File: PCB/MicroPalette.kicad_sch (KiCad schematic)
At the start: 5 parts, among them J1 Conn_01x07_Pin, J2 Conn_01x04_Pin, U1 XIAO-RP2040-DIP

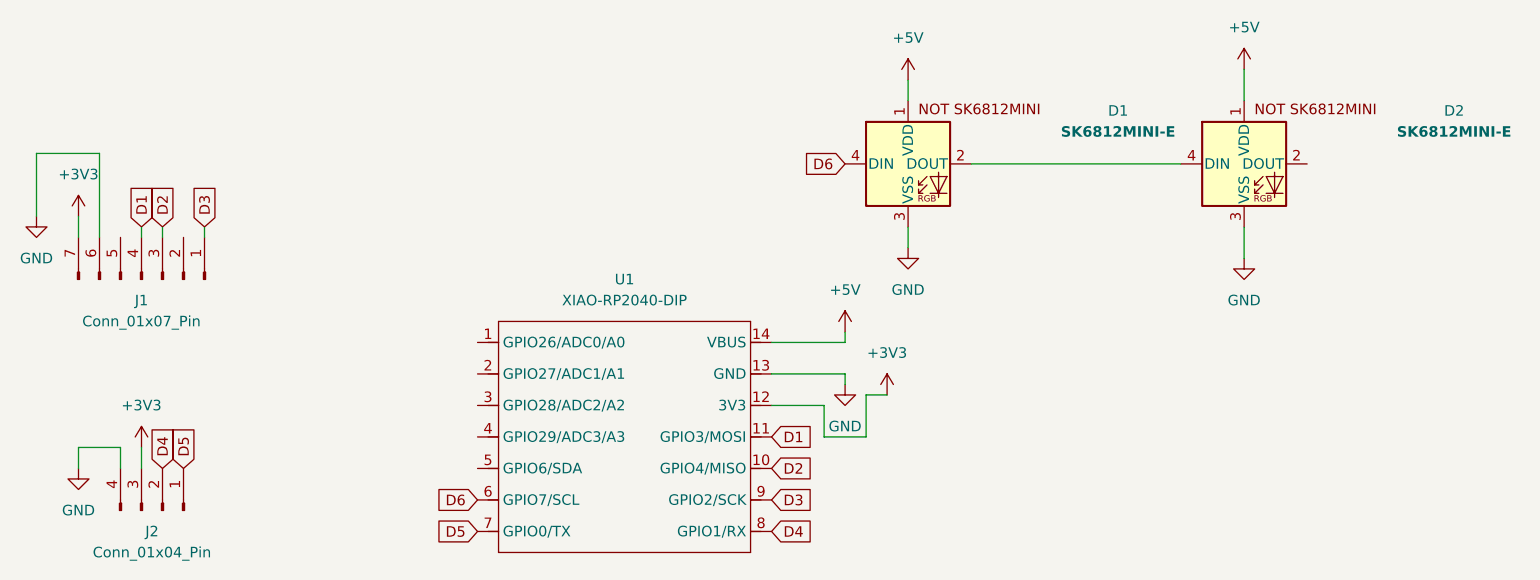
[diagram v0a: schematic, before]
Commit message: Add files via upload
fixed pcb, sda/scl was wrong in the previous version
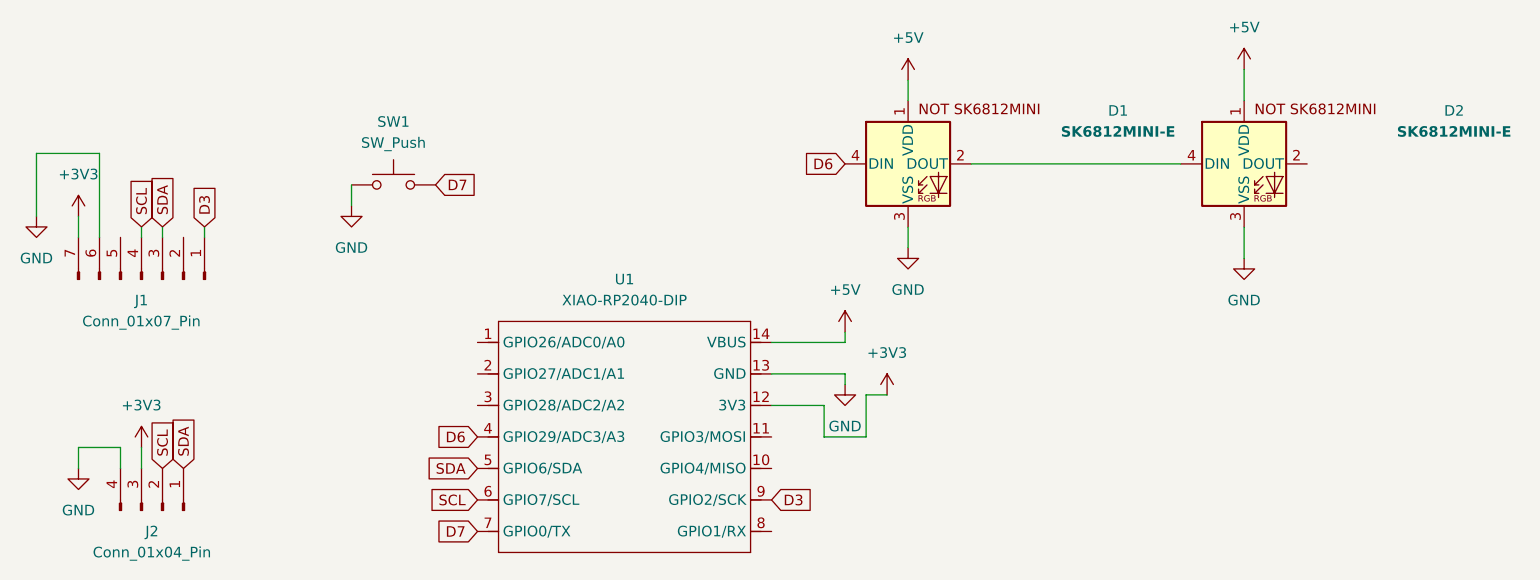
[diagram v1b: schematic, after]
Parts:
- added SW1: SW_Push, Button_Switch_Keyboard:SW_Cherry_MX_1.00u_PCB, symbol Switch:SW_Push
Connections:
- net D6: now also U1.4 (GPIO29/ADC3/A3); no longer U1.6 (GPIO7/SCL)
- net GND: now also SW1.1
- net SDA: now reaches U1.5 (GPIO6/SDA)
- net SDA: now also J1.3 (Pin_3), J2.1 (Pin_1)
- net D1: no longer names the net of U1.11 (GPIO3/MOSI)
- net D1: no longer J1.4 (Pin_4)
- net D2: no longer names the net of U1.10 (GPIO4/MISO)
- net D2: no longer J1.3 (Pin_3)
- net D4: no longer names the net of U1.8 (GPIO1/RX)
- net D4: no longer J2.2 (Pin_2)
- net D5 renamed D7
- net D7: now also SW1.2; no longer J2.1 (Pin_1)
- new net SCL: J1.4 (Pin_4), J2.2 (Pin_2), U1.6 (GPIO7/SCL)
